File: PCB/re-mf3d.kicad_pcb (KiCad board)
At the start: 2 copper layers, 136 x 135 mm, 143 parts, among them J1 USB_B, P1 Conn_02x05_Odd_Even, P2 Conn_01x06_Female, Q1 Q_NMOS_GSD, Q2 Q_NMOS_GSD, SW1 SW_Push, SW10 SW_Push, SW11 SW_Push, SW12 SW_Push, SW13 SW_Push, SW14 SW_Push, SW15 SW_Push, SW16 SW_Push, SW17 SW_Push, SW18 SW_Push, SW19 SW_Push, SW2 SW_Push, SW20 SW_Push, SW21 SW_Push, SW22 SW_Push, SW23 SW_Push, SW24 SW_Push, SW25 SW_Push, SW26 SW_Push, SW27 SW_Push, SW28 SW_Push, SW3 SW_Push, SW4 SW_Push, SW5 SW_Push, SW6 SW_Push, SW7 SW_Push, SW8 SW_Push, SW9 SW_Push, U1 PWP28_6P17X2P4, U10 ITG-3200, U11 QFN-16_3x3mm_P0.5mm, U2 PWP28_6P17X2P4, U3 PWP28_6P17X2P4, U4 MC74HC165AD, U5 MC74HC165AD, U6 MC74HC165AD, U7 MMA8453QR1, U8 ZXCL330H5TA, U9 ATmega32U4-A, X1 16MHz

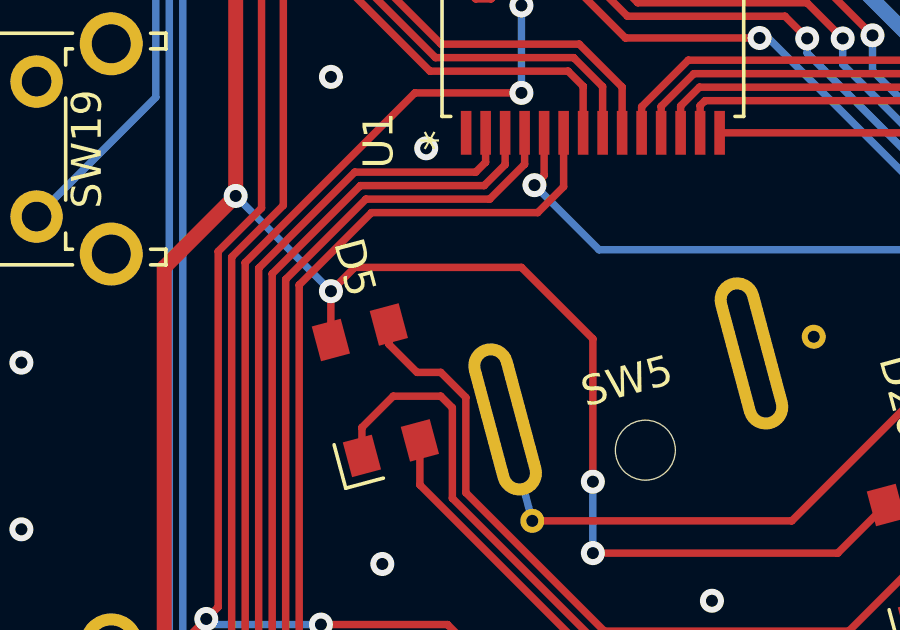
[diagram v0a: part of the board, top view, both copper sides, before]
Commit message: Added some ground fills
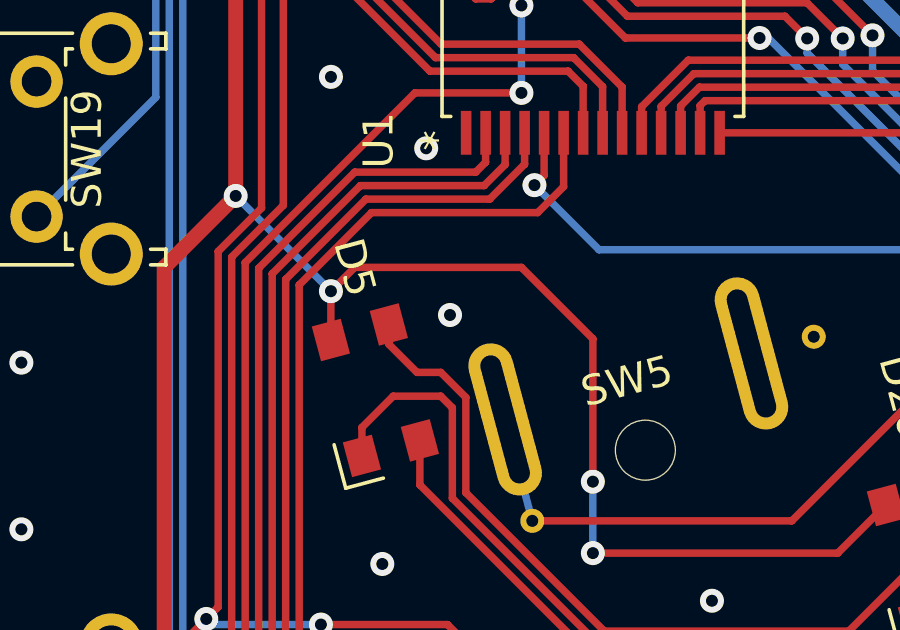
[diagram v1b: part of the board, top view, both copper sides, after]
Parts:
- U1, U2, U3: value PWP28_6P17X2P4 -> TLC59461PWP
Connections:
- J1 pad 5: unconnected-(J1-Pad5) -> GND
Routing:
- net GND: vias 247 -> 248

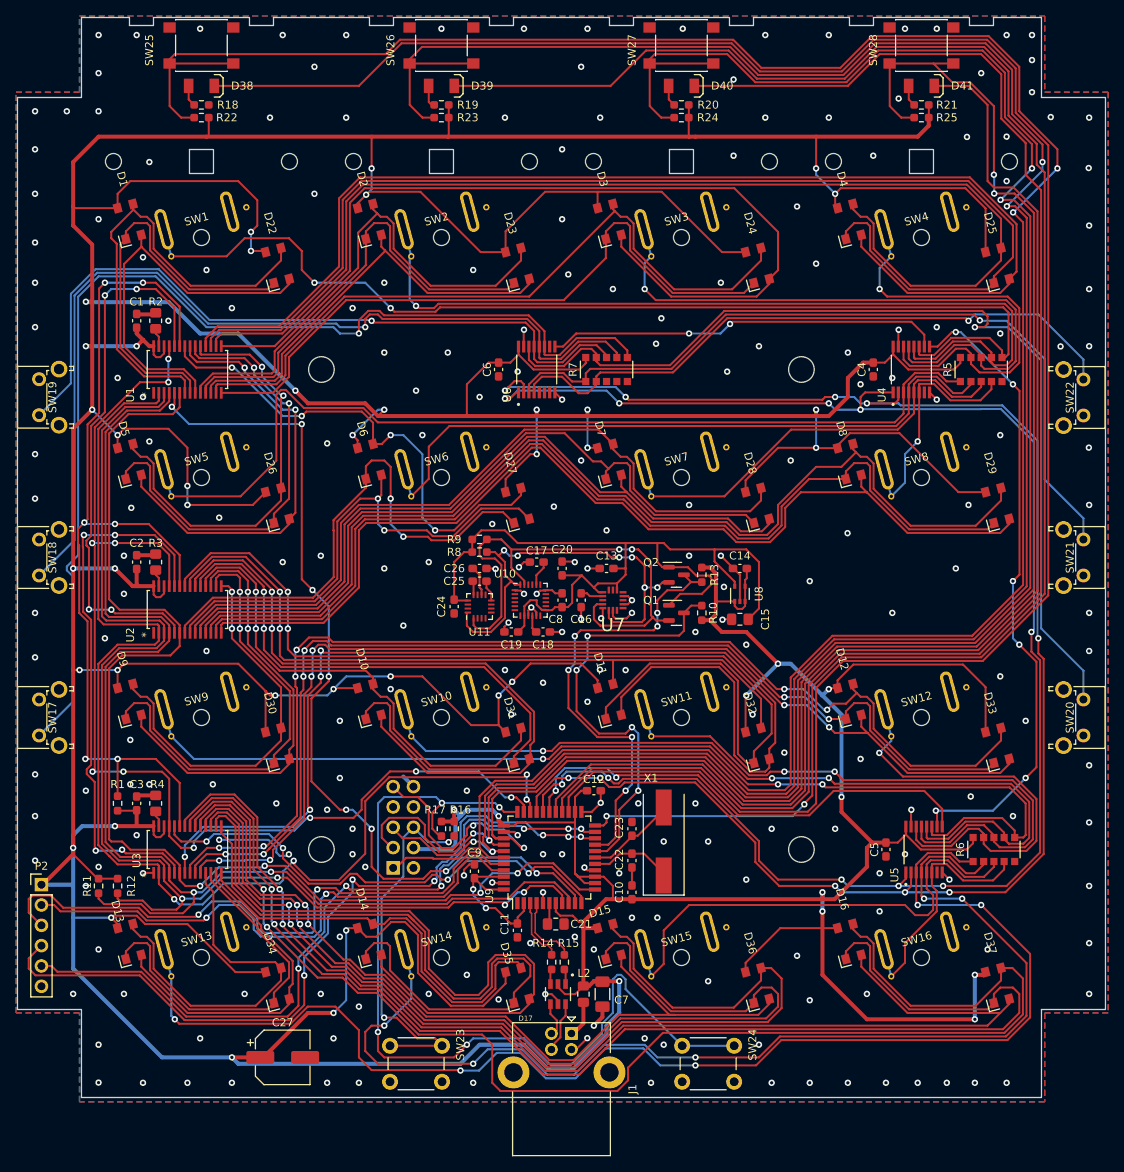
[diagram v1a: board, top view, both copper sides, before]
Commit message: Migrate to kicad7 and component updates
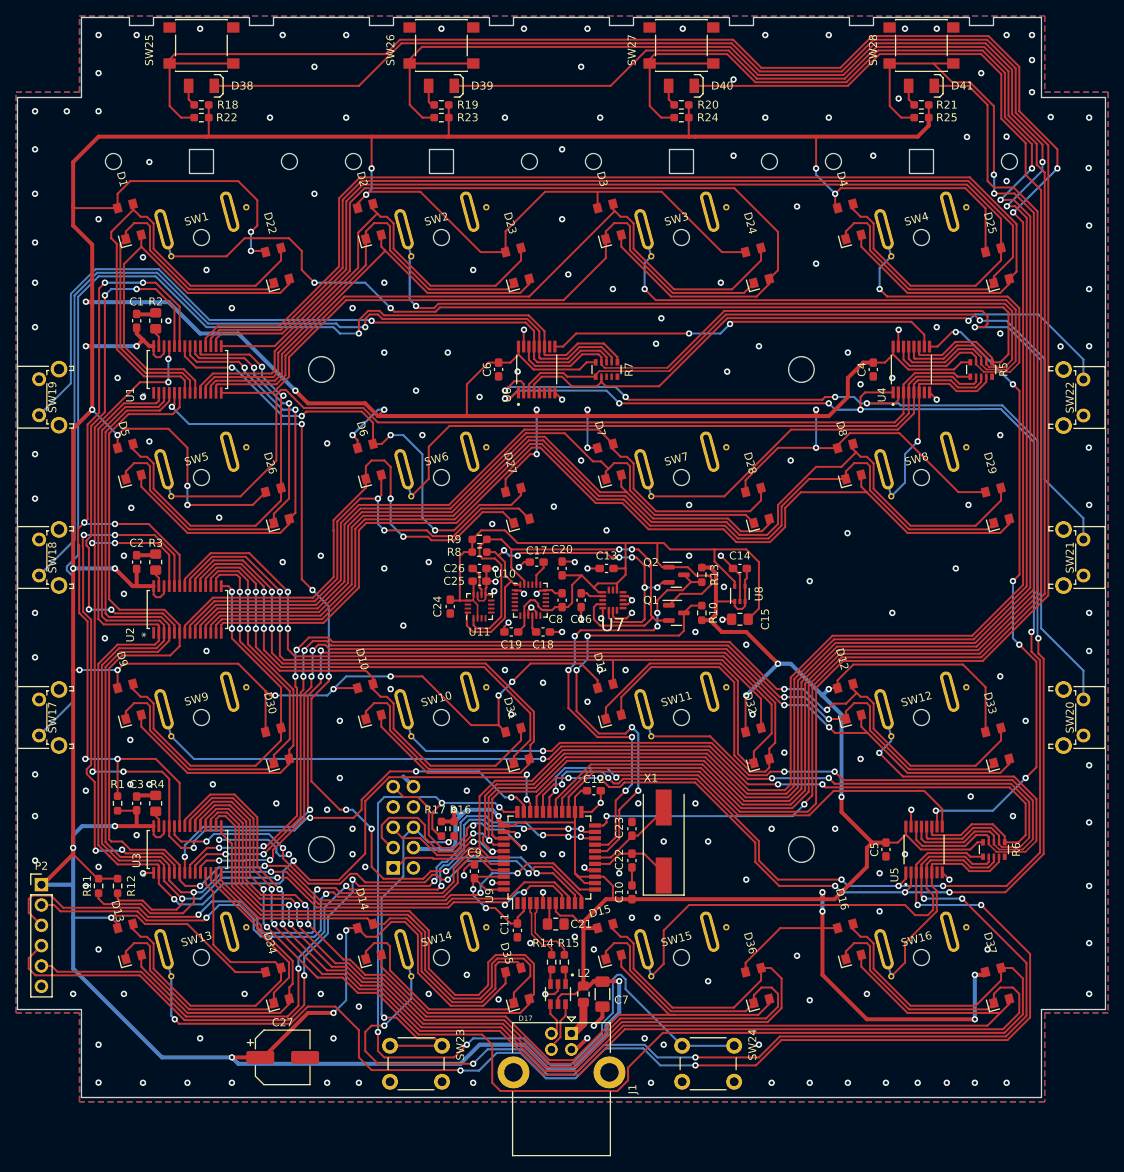
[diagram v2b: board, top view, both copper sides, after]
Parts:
- C1, C2, C24, C25, C3: value C_Small -> 0.1uF
- C22, C23: value C_Small -> 22pF
- C26: value C_Small -> 4.7uF
- L2: value L_Small -> 10mH
- R5, R6, R7: footprint assets:R_Array_Convex_5x1206_mirrored -> Resistor_SMD:R_Array_Convex_5x0603
- moved C24 0.49 mm to (128.1, 97.6)
- turned R5 to -90 degrees
- turned R6 to -90 degrees
- turned R7 to -90 degrees
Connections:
- C25 pad 1: unconnected-(C25-Pad1) -> +3V3
- C25 pad 2: unconnected-(C25-Pad2) -> GND
- C26 pad 1: unconnected-(C26-Pad1) -> Net-(U11-C1)
- D17 pad 2: +5V -> GND
- D17 pad 5: GND -> +5V
- R5 pad 1: +5V -> /buttons/U4A
- R5 pad 10: (no net) -> unconnected-(R5-Common-Pad10)
- R5 pad 2: /buttons/U4D -> /buttons/U4B
- R5 pad 4: /buttons/U4B -> /buttons/U4D
- R5 pad 5: /buttons/U4A -> +5V
- R6 pad 1: +5V -> /buttons/U5A
- R6 pad 10: (no net) -> unconnected-(R6-Common-Pad10)
- R6 pad 2: /buttons/U5D -> /buttons/U5B
- R6 pad 4: /buttons/U5B -> /buttons/U5D
- R6 pad 5: /buttons/U5A -> +5V
- R7 pad 1: +5V -> /buttons/U6A
- R7 pad 10: (no net) -> unconnected-(R7-Common-Pad10)
- R7 pad 2: /buttons/U6D -> /buttons/U6B
- R7 pad 4: /buttons/U6B -> /buttons/U6D
- R7 pad 5: /buttons/U6A -> +5V
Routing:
- net GND: track 84.2 -> 92.8 mm, vias 248 -> 250
- net +3V3: track 111.0 -> 116.7 mm
- net +5V: track 1247.4 -> 1251.3 mm
- net unconnected-(C26-Pad1): track 3.73 -> 0.00 mm
- net Net-(U11-C1): track 0.00 -> 3.73 mm
- net unconnected-(C25-Pad2): track 2.67 -> 0.00 mm
- net /buttons/U6A: track 138.7 -> 137.1 mm
- net unconnected-(C25-Pad1): track 1.60 -> 0.00 mm
- net /buttons/U5H: track 32.0 -> 30.4 mm
- net /buttons/U4H: track 30.8 -> 29.2 mm
- net /buttons/U4E: track 119.7 -> 120.7 mm
- net /buttons/U5E: track 167.7 -> 168.7 mm
- net /buttons/U6E: track 97.4 -> 96.5 mm
- net /buttons/U6B: track 116.2 -> 115.3 mm
- net /buttons/U5D: track 54.1 -> 53.4 mm
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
